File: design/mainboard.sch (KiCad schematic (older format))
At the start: 0 parts

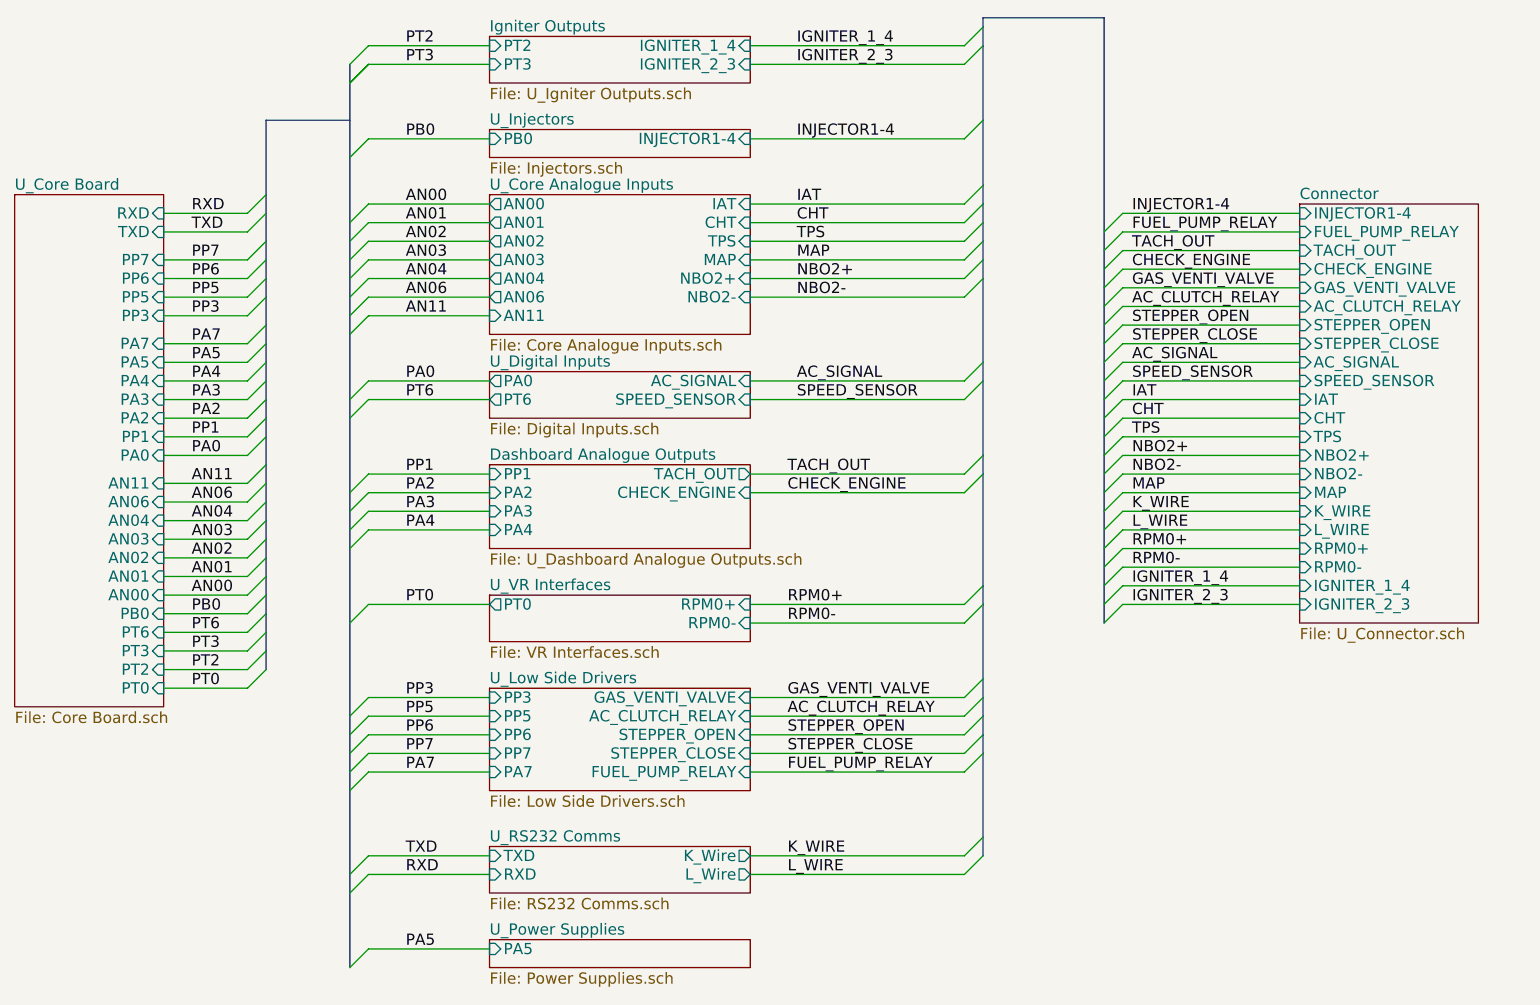
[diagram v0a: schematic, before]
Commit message: revise schema according to Jaguar & Ravage project, eliminate as many errors as possible which were inherited from Puma board. Remove VSS interface, narrow band O2 interface, AC relay output, AC signal input. Make fuel injection configurable which can be batch fired or semi sequential fired
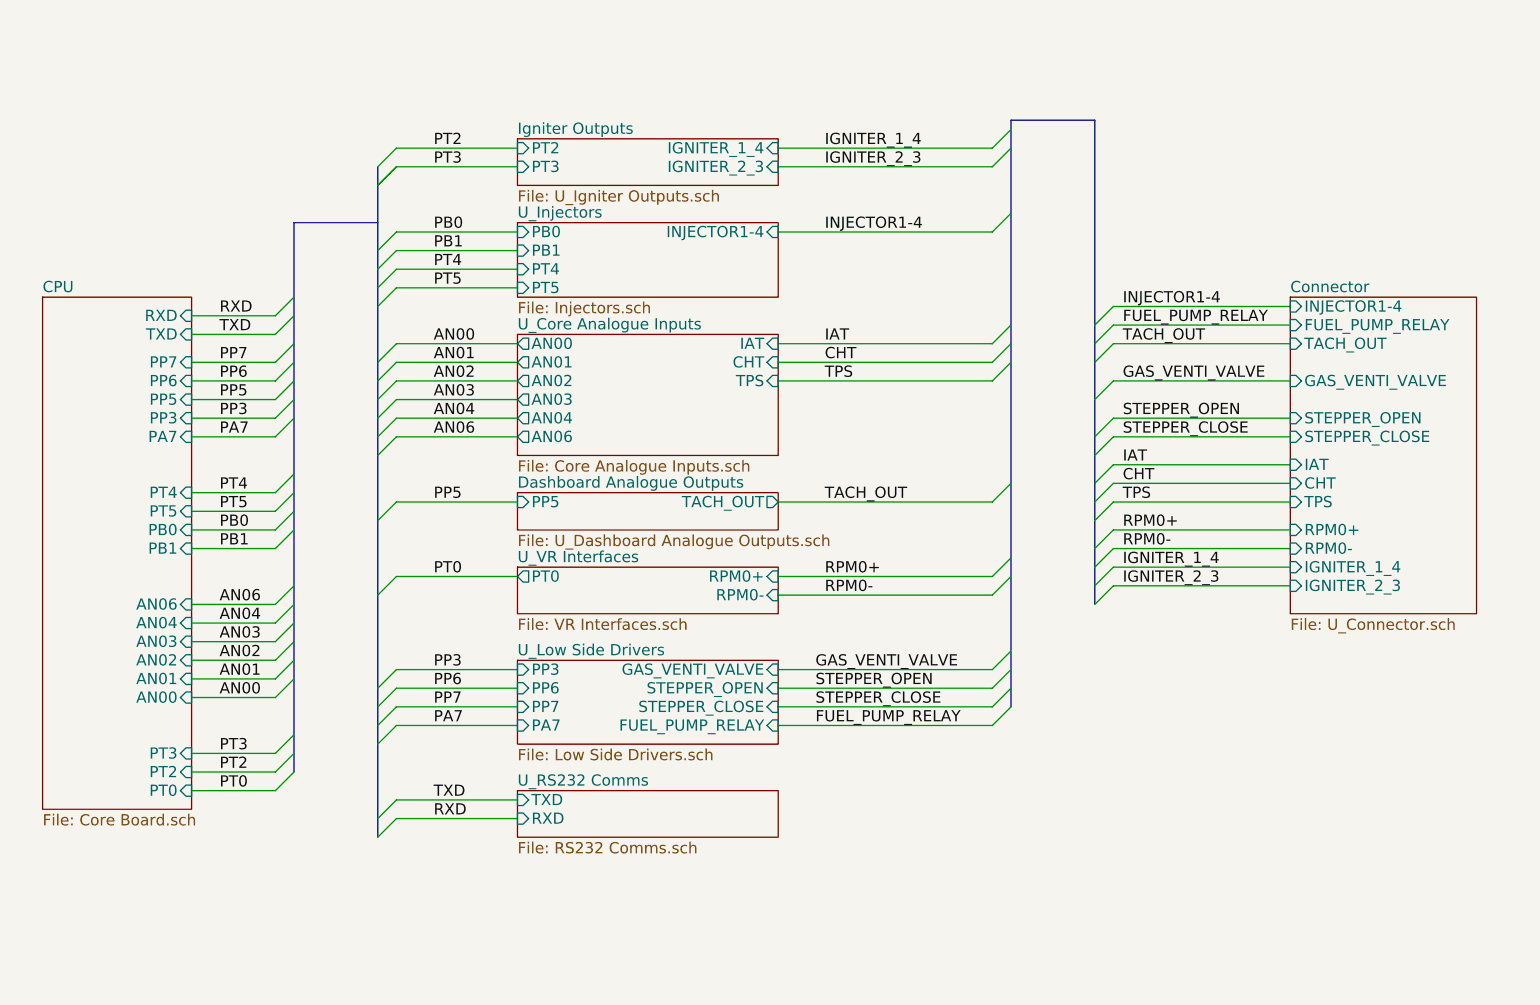
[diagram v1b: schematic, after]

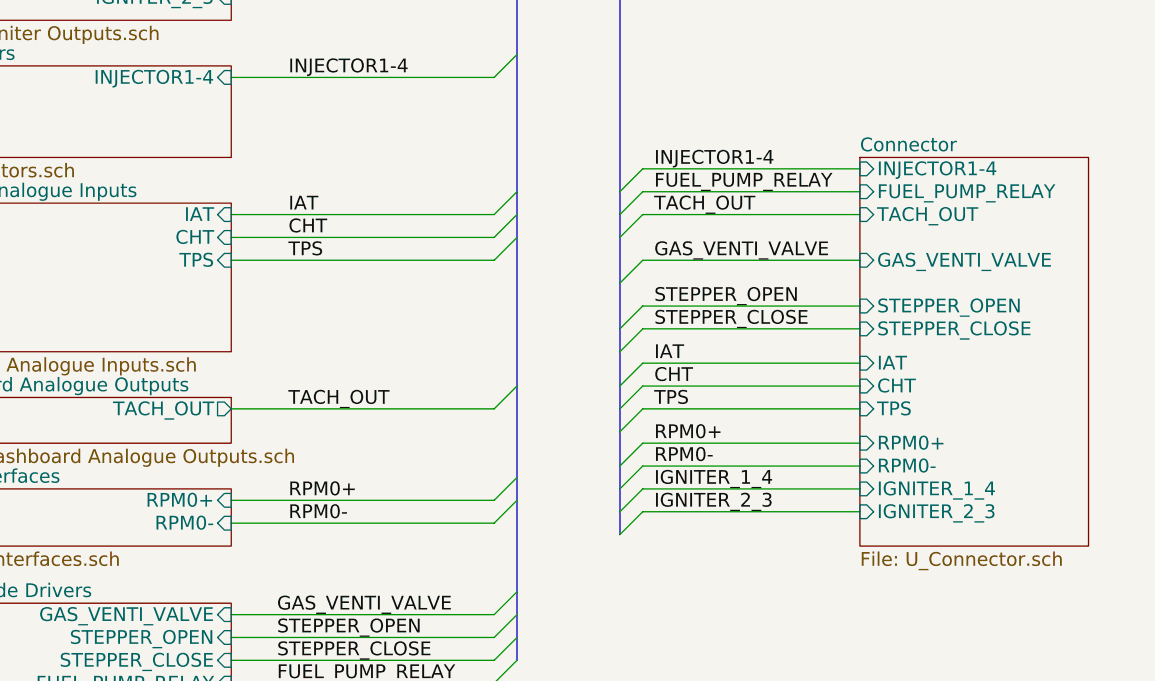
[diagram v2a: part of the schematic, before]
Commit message: make new footprint for screw connector, redesign ignition gnd & all lowside gnd
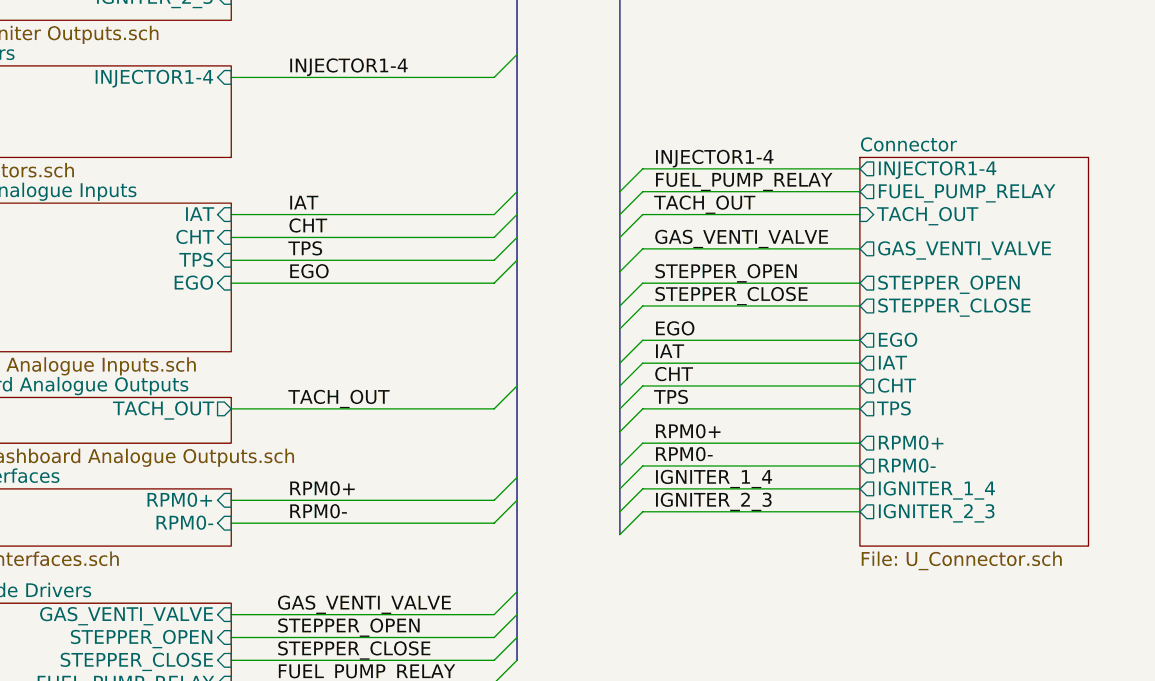
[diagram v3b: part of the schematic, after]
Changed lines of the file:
@@
-EESchema Schematic File Version 2  date 02/02/2012 10:58:16
+EESchema Schematic File Version 2  date 07/02/2012 00:44:28
 LIBS:power
 LIBS:device
@@
 Sheet 1 10
 Title "CatSquirt main board(code migrant worker)"
-Date "2 feb 2012"
+Date "6 feb 2012"
 Rev "0.01"
 Comp "diyefi.org"
@@
 Comment4 ""
 $EndDescr
+$Sheet
+S 8650 2900 1000 1700
+U 4E951714
+F0 "Connector" 60
+F1 "U_Connector.sch" 60
+F2 "TPS" O L 8650 4000 60
+F3 "CHT" O L 8650 3900 60
+F4 "IAT" O L 8650 3800 60
+F5 "RPM0-" O L 8650 4250 60
+F6 "INJECTOR1-4" O L 8650 2950 60
+F7 "FUEL_PUMP_RELAY" O L 8650 3050 60
+F8 "TACH_OUT" I L 8650 3150 60
+F9 "GAS_VENTI_VALVE" O L 8650 3300 60
+F10 "STEPPER_OPEN" O L 8650 3450 60
+F11 "STEPPER_CLOSE" O L 8650 3550 60
+F12 "EGO" O L 8650 3700 60
+F13 "RPM0+" O L 8650 4150 60
+F14 "IGNITER_1_4" O L 8650 4350 60
+F15 "IGNITER_2_3" O L 8650 4450 60
+$EndSheet
+Wire Wire Line
+	7700 3700 8650 3700
+Wire Wire Line
+	7700 3300 8650 3300
 Wire Wire Line
 	2750 4250 3200 4250
@@
 	8650 3150 7700 3150
 Wire Wire Line
-	8650 3350 7700 3350
-Wire Wire Line
 	8650 3550 7700 3550
 Wire Wire Line
-	8650 3650 7700 3650
-Wire Wire Line
 	2750 5550 3200 5550
 Wire Wire Line
@@
 Wire Wire Line
 	2750 4050 3200 4050
+Wire Wire Line
+	5900 3450 7050 3450
+Wire Wire Line
+	7700 3450 8650 3450
+Text Label 7750 3700 0    60   ~ 0
+EGO
+Entry Wire Line
+	7600 3550 7700 3450
+Text Label 6150 3450 0    60   ~ 0
+EGO
+Entry Wire Line
+	7050 3450 7150 3350
 $Sheet
 S 1950 2900 800  2750
@@
 	3750 2850 3850 2750
 $Sheet
-S 8650 2900 1000 1700
-U 4E951714
-F0 "Connector" 60
-F1 "U_Connector.sch" 60
-F2 "FUEL_PUMP_RELAY" I L 8650 3050 60
-F3 "STEPPER_CLOSE" I L 8650 3650 60
-F4 "STEPPER_OPEN" I L 8650 3550 60
-F5 "GAS_VENTI_VALVE" I L 8650 3350 60
-F6 "RPM0-" I L 8650 4250 60
-F7 "RPM0+" I L 8650 4150 60
-F8 "TACH_OUT" I L 8650 3150 60
-F9 "TPS" I L 8650 4000 60
-F10 "CHT" I L 8650 3900 60
-F11 "IAT" I L 8650 3800 60
-F12 "INJECTOR1-4" I L 8650 2950 60
-F13 "IGNITER_2_3" I L 8650 4450 60
-F14 "IGNITER_1_4" I L 8650 4350 60
-$EndSheet
-$Sheet
 S 4500 3950 1400 200
 U 4E939ACE
@@
 F9 "AN00" O L 4500 3150 60
 F10 "AN06" O L 4500 3650 60
+F11 "EGO" I R 5900 3450 60
 $EndSheet
 Entry Wire Line
@@
 Text Label 7750 3800 0    60   ~ 0
 IAT
-Text Label 7750 3650 0    60   ~ 0
+Text Label 7750 3550 0    60   ~ 0
 STEPPER_CLOSE
-Text Label 7750 3550 0    60   ~ 0
+Text Label 7750 3450 0    60   ~ 0
 STEPPER_OPEN
-Text Label 7750 3350 0    60   ~ 0
+Text Label 7750 3300 0    60   ~ 0
 GAS_VENTI_VALVE
 Text Label 7750 3150 0    60   ~ 0
@@
 	7600 3900 7700 3800
 Entry Wire Line
-	7600 3750 7700 3650
+	7600 3800 7700 3700
 Entry Wire Line
 	7600 3650 7700 3550
 Entry Wire Line
-	7600 3450 7700 3350
+	7600 3400 7700 3300
 Entry Wire Line
 	7600 3250 7700 3150
